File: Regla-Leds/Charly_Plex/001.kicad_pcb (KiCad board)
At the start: 2 copper layers, 49.7 x 49.3 mm, 20 parts, among them J2 Conn_01x08, U1 PCB

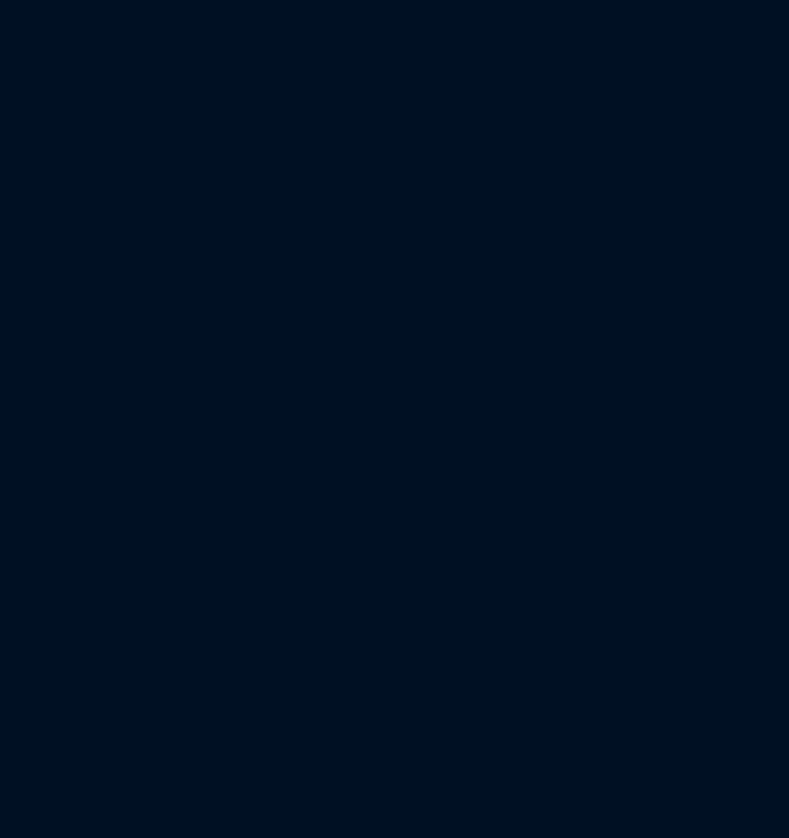
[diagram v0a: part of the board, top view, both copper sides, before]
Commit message: Add Digispark Footprint
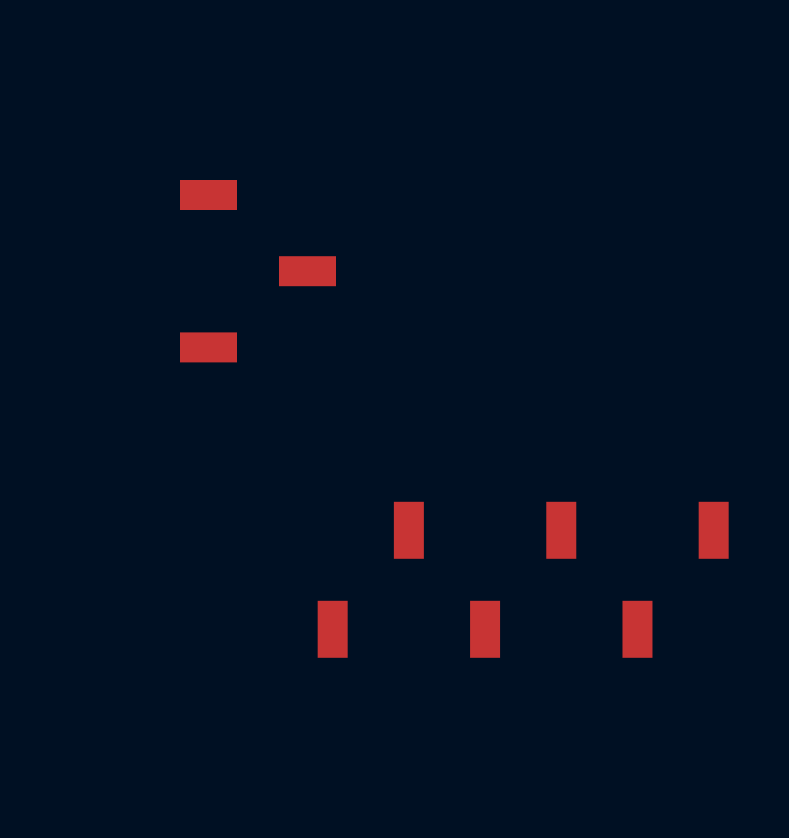
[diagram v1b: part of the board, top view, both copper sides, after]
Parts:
- added REF**: Digispark_SMD, Reverse_Mount_Leds:Digispark_SMD, F.Cu at (248.9, 96.5)
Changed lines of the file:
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@@
     (tracks 90)
     (zones 0)
-    (modules 20)
+    (modules 21)
     (nets 15)
   )
@@
     (uvia_drill 0.508)
   )
+  (module Reverse_Mount_Leds:Digispark_SMD (layer F.Cu)
+    (at 248.92 96.52)
+    (fp_text reference REF** (at 0.0508 14.4018 -180) (layer F.Fab)
+      (effects (font (size 1 1) (thickness 0.15)))
+    )
+    (fp_text value Digispark_SMD (at -0.1524 15.5702) (layer F.Fab)
+      (effects (font (size 1 1) (thickness 0.15)))
+    )
+    (fp_circle (center 6.340974 10.16) (end 7.239 10.16) (layer F.Fab) (width 0.12))
+    (fp_circle (center 3.826374 10.16) (end 4.7244 10.16) (layer F.Fab) (width 0.12))
+    (fp_circle (center 1.260974 10.16) (end 2.159 10.16) (layer F.Fab) (width 0.12))
+    (fp_circle (center -1.279026 10.16) (end -0.381 10.16) (layer F.Fab) (width 0.12))
+    (fp_circle (center -3.819026 10.16) (end -2.921 10.16) (layer F.Fab) (width 0.12))
+    (fp_circle (center -6.359026 10.1346) (end -5.461 10.1346) (layer F.Fab) (width 0.12))
+    (fp_circle (center -8.8646 2.413) (end -7.966574 2.413) (layer F.Fab) (width 0.12))
+    (fp_circle (center -8.8646 -0.127) (end -7.966574 -0.127) (layer F.Fab) (width 0.12))
+    (fp_circle (center -8.8646 -2.6924) (end -7.966574 -2.6924) (layer F.Fab) (width 0.12))
+    (fp_line (start -10.6 11.91) (end 8.4 11.91) (layer F.Fab) (width 0.15))
+    (fp_line (start -7.06 -5.59) (end -10.6 -5.59) (layer F.Fab) (width 0.15))
+    (fp_line (start 4.97 -14.59) (end 4.97 -5.59) (layer F.Fab) (width 0.15))
+    (fp_line (start 4.97 -14.59) (end -7.06 -14.59) (layer F.Fab) (width 0.15))
+    (fp_line (start -10.6 -5.59) (end -10.6 11.91) (layer F.Fab) (width 0.15))
+    (fp_line (start 4.97 -5.59) (end 8.4 -5.59) (layer F.Fab) (width 0.15))
+    (fp_line (start 8.4 -5.59) (end 8.4 11.91) (layer F.Fab) (width 0.15))
+    (fp_line (start -7.06 -14.59) (end -7.06 -5.59) (layer F.Fab) (width 0.15))
+    (pad 6 smd rect (at 6.35 8.51 270) (size 1.9 1) (layers F.Cu F.Paste F.Mask))
+    (pad 5 smd rect (at 3.81 11.81 270) (size 1.9 1) (layers F.Cu F.Paste F.Mask))
+    (pad 4 smd rect (at 1.27 8.51 270) (size 1.9 1) (layers F.Cu F.Paste F.Mask))
+    (pad 3 smd rect (at -1.27 11.81 270) (size 1.9 1) (layers F.Cu F.Paste F.Mask))
+    (pad 2 smd rect (at -3.81 8.51 270) (size 1.9 1) (layers F.Cu F.Paste F.Mask))
+    (pad 1 smd rect (at -6.35 11.81 270) (size 1.9 1) (layers F.Cu F.Paste F.Mask))
+    (pad 7 smd rect (at -10.4892 2.413) (size 1.9 1) (layers F.Cu F.Paste F.Mask))
+    (pad 8 smd rect (at -7.1892 -0.127) (size 1.9 1) (layers F.Cu F.Paste F.Mask))
+    (pad 9 smd rect (at -10.4892 -2.667) (size 1.9 1) (layers F.Cu F.Paste F.Mask))
+    (model ${KISYS3DMOD}/Connector_PinSocket_2.54mm.3dshapes/PinSocket_1x03_P2.54mm_Vertical_SMD_Pin1Right.wrl
+      (offset (xyz -8.800000000000001 0.13 0))
+      (scale (xyz 1 1 1))
+      (rotate (xyz 0 0 180))
+    )
+    (model ${KISYS3DMOD}/Connector_PinSocket_2.54mm.3dshapes/PinSocket_1x06_P2.54mm_Vertical_SMD_Pin1Left.wrl
+      (offset (xyz 0 -10.1 0))
+      (scale (xyz 1 1 1))
+      (rotate (xyz 0 0 90))
+    )
+  )
   (module Connector_PinSocket_2.54mm:PinSocket_1x06_P2.54mm_Vertical_SMD_Pin1Left (layer F.Cu)
     (at 222.885 106.68 90)
@@
     (pad 2 thru_hole circle (at -3.81 0) (size 1.8796 1.8796) (drill 1.016) (layers *.Cu *.Mask))
     (pad 1 thru_hole circle (at -6.35 0) (size 1.8796 1.8796) (drill 1.016) (layers *.Cu *.Mask))
+    (model "${KISYS3DMOD}/Module.3dshapes/DigiSpark ATtiny85.STEP"
+      (offset (xyz -36 50.1 -10))
+      (scale (xyz 1 1 1))
+      (rotate (xyz 0 0 90))
+    )
   )
   (module Reverse_Mount_Leds:LED_D5.0mm_Reverse (layer B.Cu)
